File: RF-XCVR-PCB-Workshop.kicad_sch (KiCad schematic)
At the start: 24 parts, among them J3 Conn_Coaxial, J4 Conn_01x12_Pin, U1 CC1101RGP, Y1 NX3225GA-26MHZ-TI

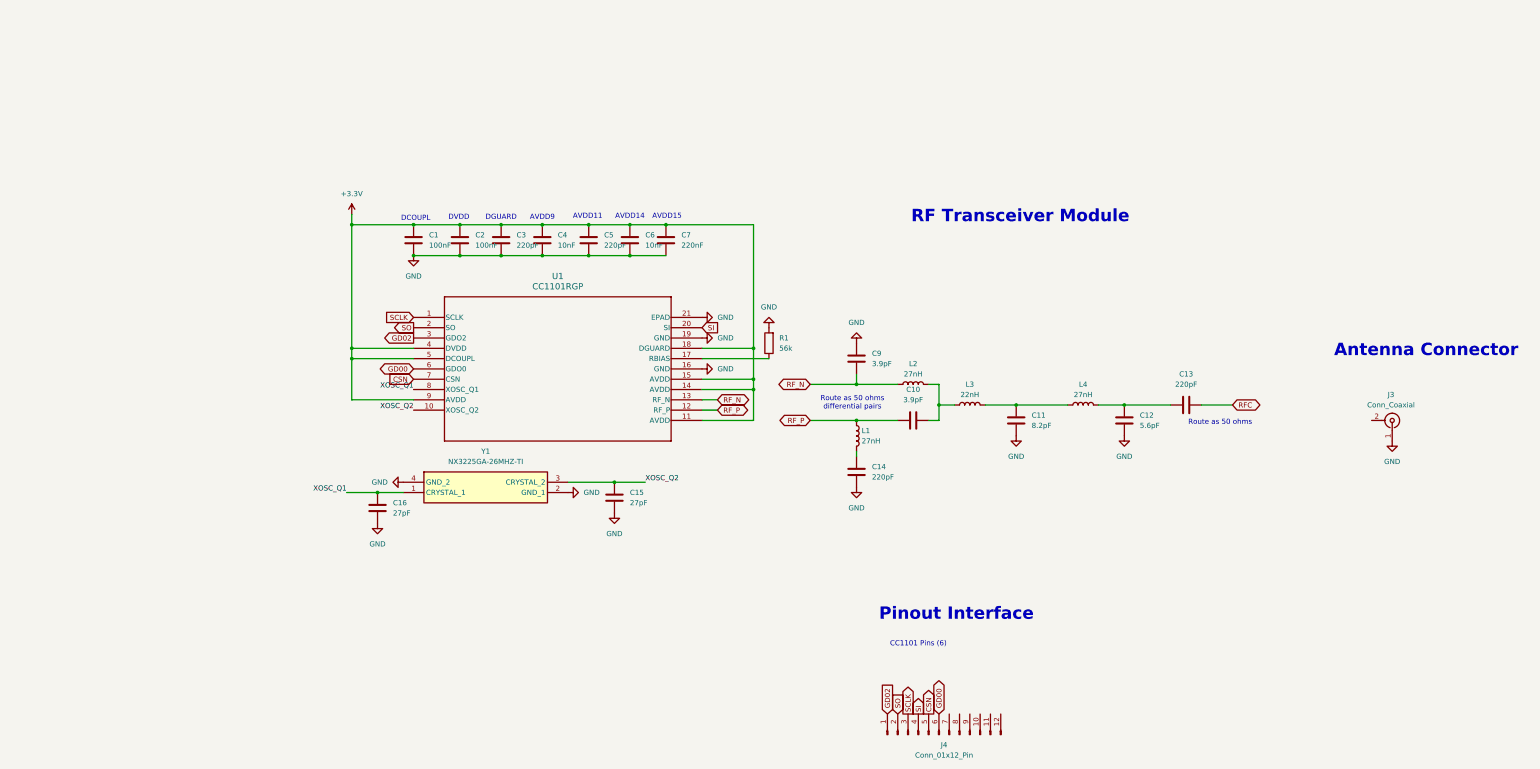
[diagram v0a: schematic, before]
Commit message: bare CC1101 XCVR laid out
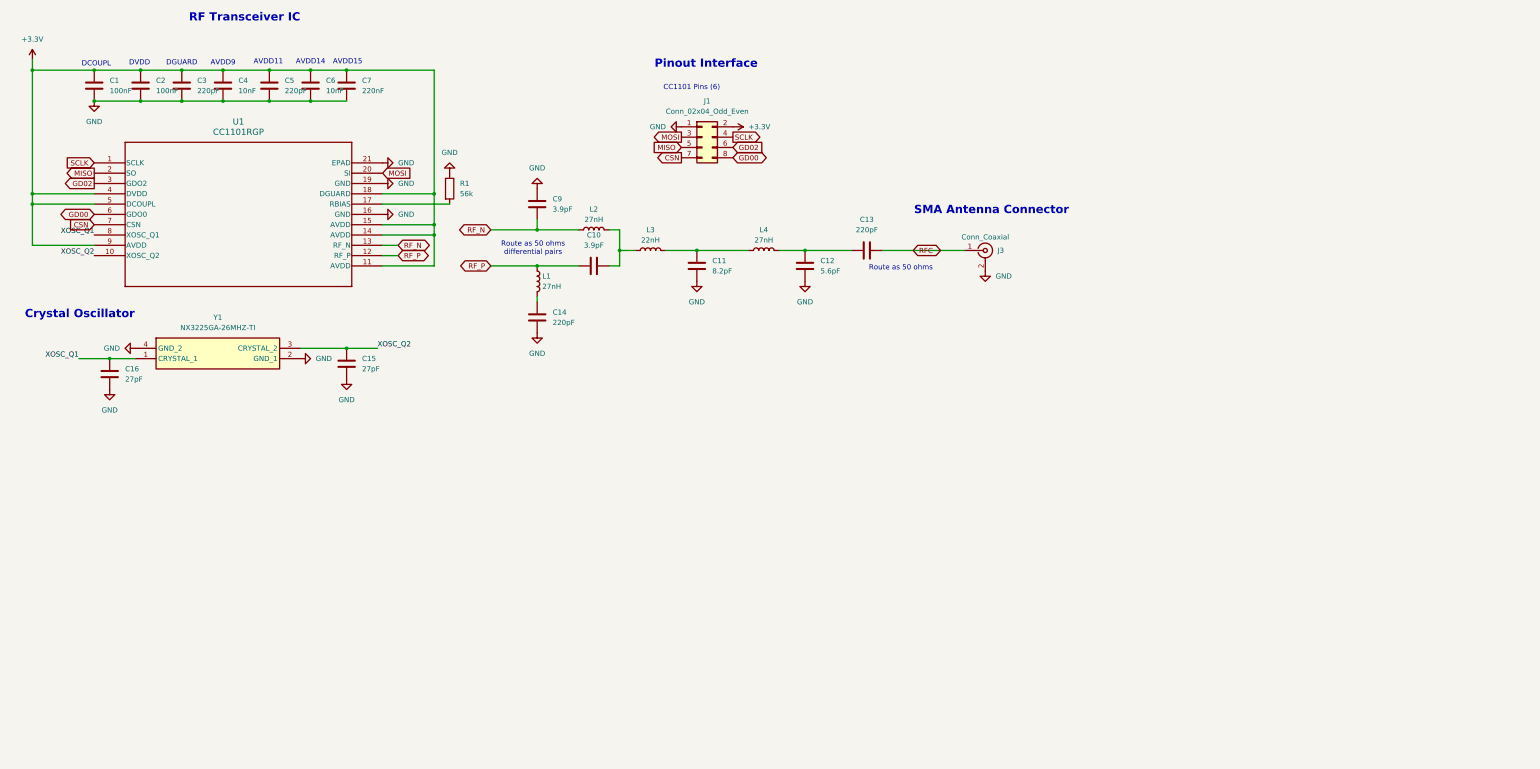
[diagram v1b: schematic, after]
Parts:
- removed J4: Conn_01x12_Pin, Connector_PinSocket_2.54mm:PinSocket_1x12_P2.54mm_Vertical, symbol Connector:Conn_01x12_Pin
- added J1: Conn_02x04_Odd_Even, Connector_PinHeader_2.54mm:PinHeader_2x04_P2.54mm_Vertical, symbol Connector_Generic:Conn_02x04_Odd_Even
- C1, C11, C12, C13, C14, C15, C16, C2, C3, C4, C5, C6, C7: footprint comms-board-footprints-passives:G-188_MUR-L-100nF-GRM188 -> Capacitor_SMD:C_0402_1005Metric
- C10, C9: footprint comms-board-footprints-passives:CAP_600S0R1AT250XT_ATC -> Capacitor_SMD:C_0402_1005Metric
- J3: footprint Connector_Coaxial:SMA_Amphenol_132134-11_Vertical -> Connector_Coaxial:SMA_Molex_73251-1153_EdgeMount_Horizontal
- L1, L2, L3, L4: footprint comms-board-footprints-passives:INDC1005X55N -> Inductor_SMD:L_0402_1005Metric
- R1: footprint comms-board-footprints-passives:RESC2012X60N -> Resistor_SMD:R_0402_1005Metric; LCSC Part # C137509 -> (none); Manufacturer_Name YAGEO -> (none); Manufacturer_Part_Number YAGEO RC0805FR-0756KL -> (none); Vendor LCSC -> (none)
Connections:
- net +3.3V: now also J1.2 (Pin_2)
- net CSN: now also J1.7 (Pin_7)
- net GD00: now also J1.8 (Pin_8)
- net GD02: now also J1.6 (Pin_6)
- net GND: now also J3.2 (Ext), R1.1, J1.1 (Pin_1); no longer J3.1 (In), R1.2
- net RFC: now also J3.1 (In)
- net SCLK: now also J1.4 (Pin_4)
- net at U1.17 (RBIAS): now also R1.2; no longer R1.1
- net SI renamed MOSI
- net MOSI: now also J1.3 (Pin_3)
- net SO renamed MISO
- net MISO: now also J1.5 (Pin_5)
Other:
- note added: "Crystal Oscillator"
- note added: "RF Transceiver IC"
- note added: "SMA Antenna Connector"
- note removed: "Antenna Connector"
- note removed: "RF Transceiver Module"
- moved on the sheet: C1, C10, C11, C12, C13, C14, C15, C16, C2, C3, C4, C5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
